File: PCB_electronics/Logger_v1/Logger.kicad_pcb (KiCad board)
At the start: 2 copper layers, 87.5 x 52.5 mm, 26 parts, among them P1 GPS_breakout_connector, P10 CONN_01X03, P11 CONN_01X02, P12 CONN_01X02, P13 CONN_01X02, P14 CONN_01X02, P15 CONN_01X02, P2 SD_breakout_connector, P3 Iridium_connector, P4 VN100_connector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

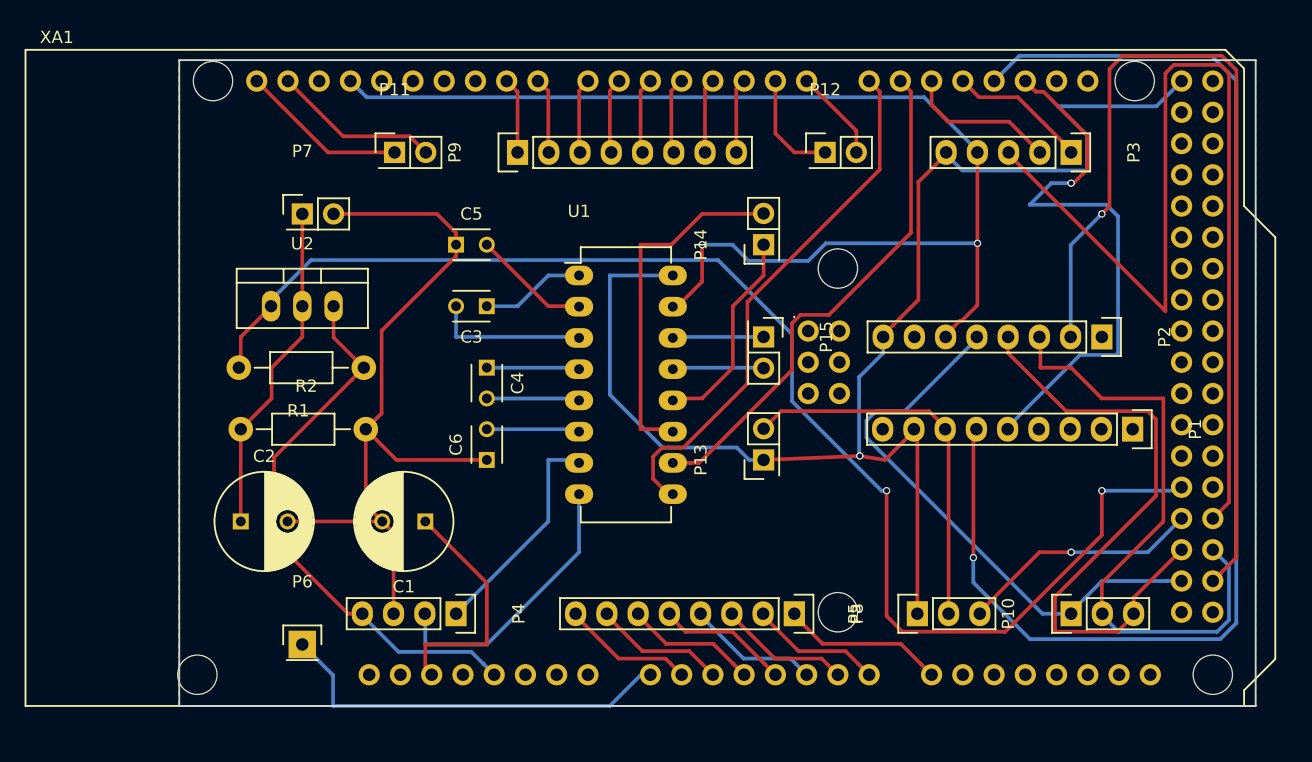
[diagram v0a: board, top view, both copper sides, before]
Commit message: corrected error on MAX232
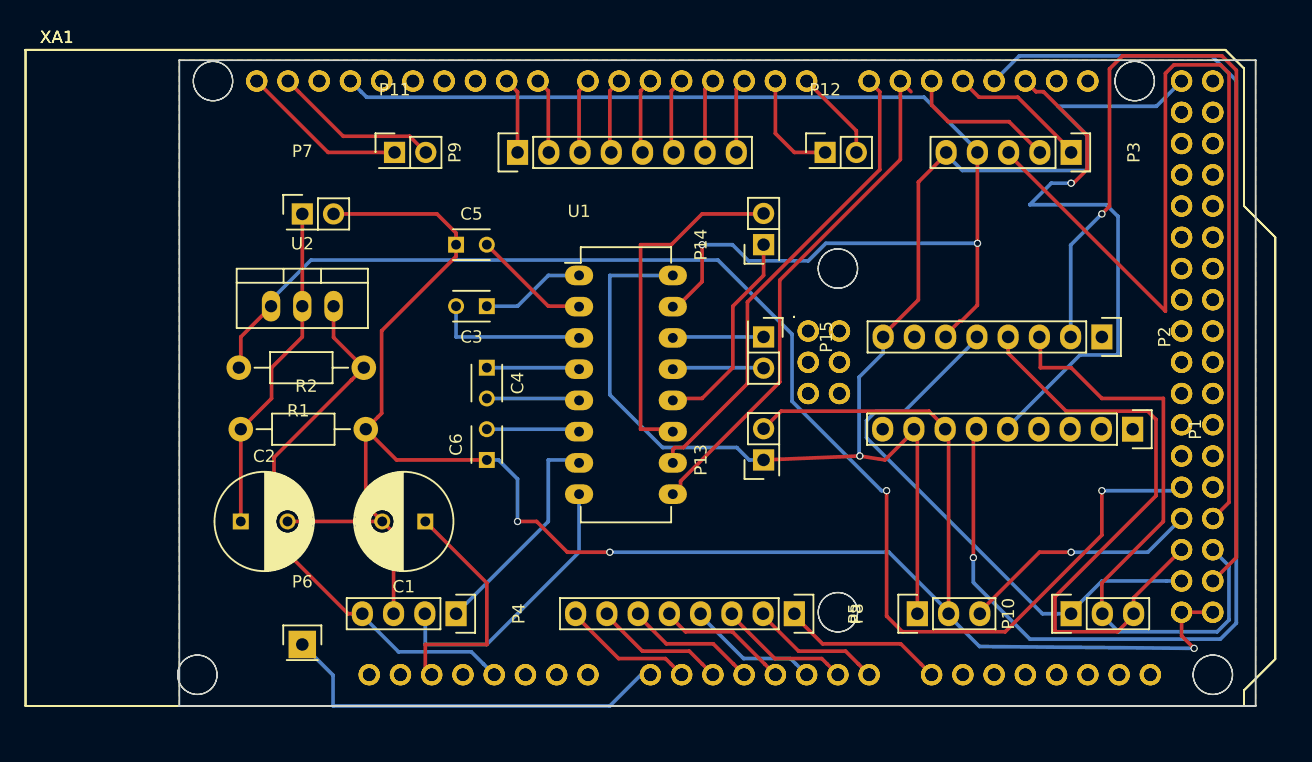
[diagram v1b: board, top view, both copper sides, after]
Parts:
- added XA1: Arduino_Mega2560_Shield, Arduino:Arduino_Mega2560_Shield, F.Cu at (112.5, 140.0)
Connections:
- U1 pad 10: /RX3 -> /TX3
- U1 pad 9: /TX3 -> /RX3
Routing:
- net GND: track 194.6 -> 266.5 mm, vias 2 -> 5
- net /TX3: track 43.5 -> 38.8 mm
- net /RX3: track 42.0 -> 42.7 mm

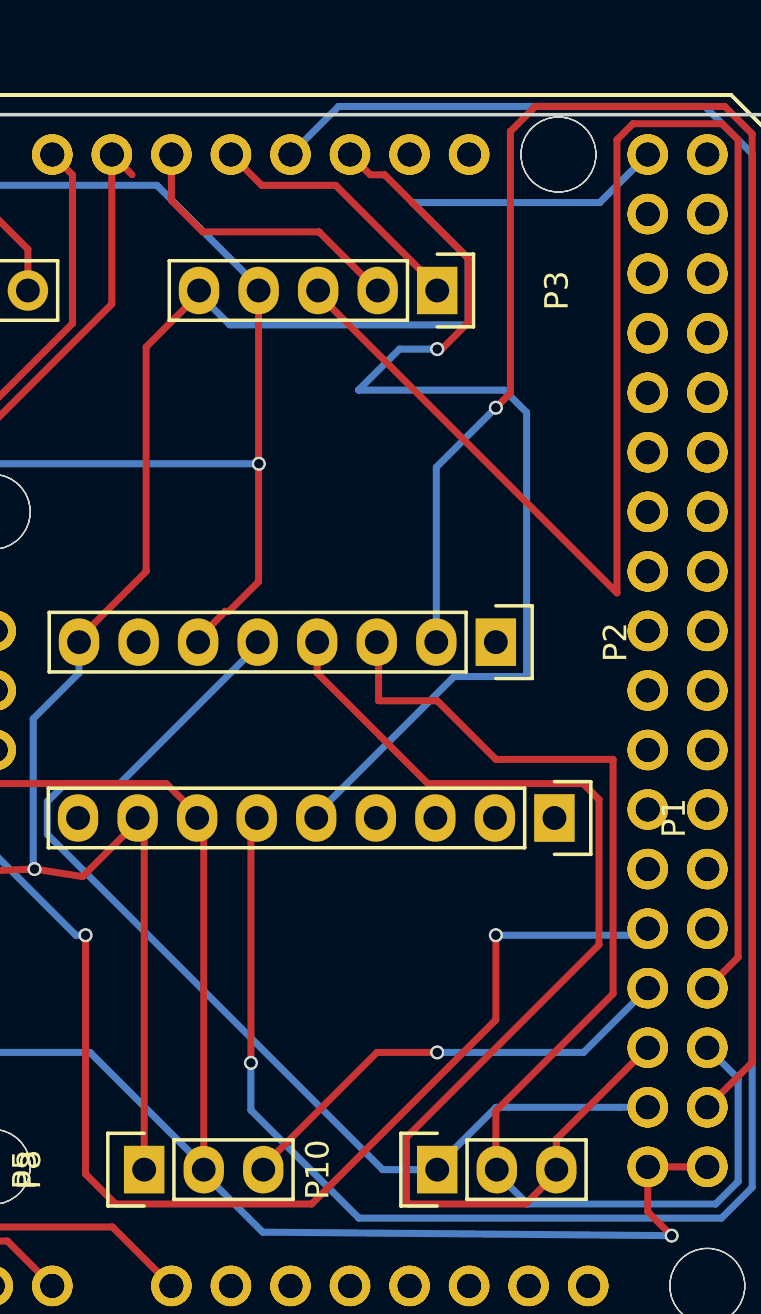
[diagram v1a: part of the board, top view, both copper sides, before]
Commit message: drc warning but should be ok
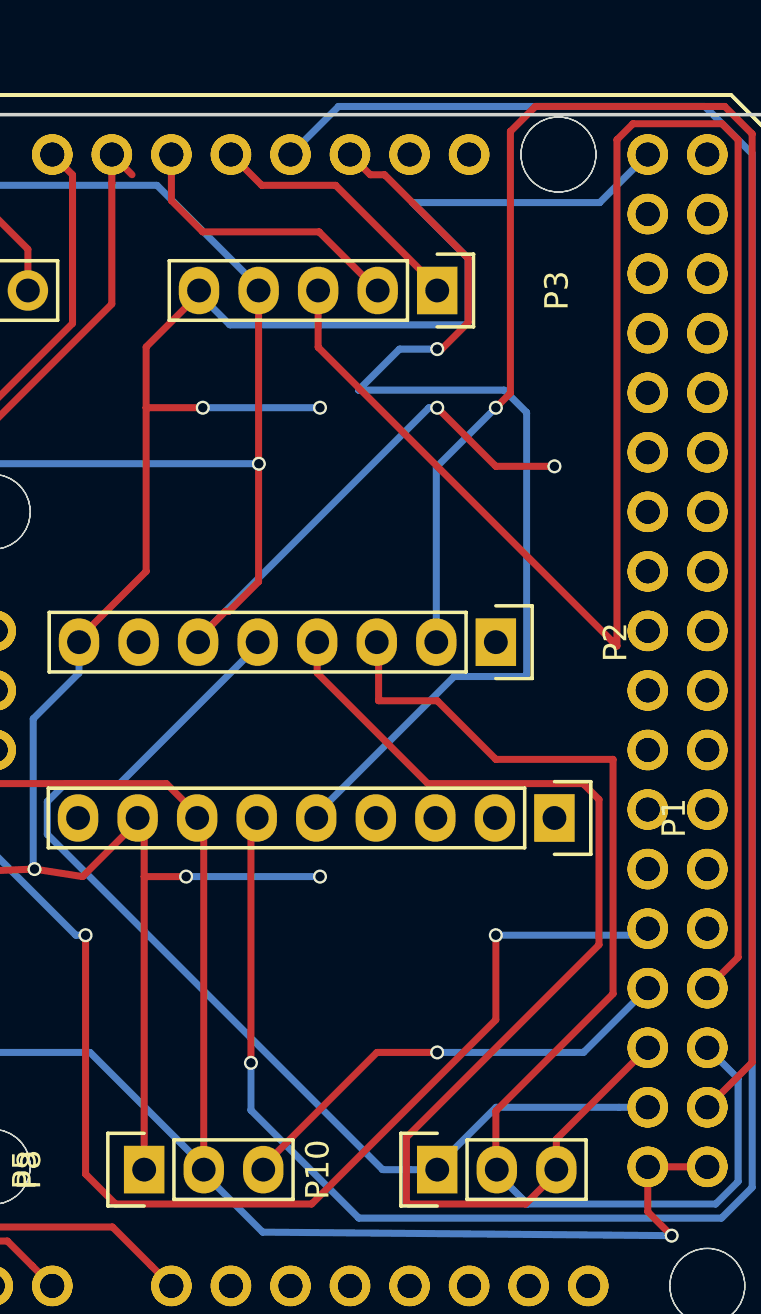
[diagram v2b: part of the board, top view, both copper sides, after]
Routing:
- net GND: track 266.5 -> 287.0 mm, vias 5 -> 7
- net +5V: track 160.4 -> 175.3 mm, vias 1 -> 5
- net /IRD_ON_OFF: track 80.0 -> 84.5 mm
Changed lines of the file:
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@@
 (kicad_pcb (version 4) (host pcbnew 4.0.2+dfsg1-stable)
   (general
-    (links 82)
+    (links 173)
     (no_connects 0)
     (area 124.924999 87.424999 212.575001 140.075001)
     (thickness 1.6)
     (drawings 4)
-    (tracks 369)
+    (tracks 386)
     (zones 0)
     (modules 27)
@@
   (gr_line (start 212.5 87.5) (end 212.5 140) (angle 90) (layer Edge.Cuts) (width 0.15))
   (gr_line (start 125 87.5) (end 212.5 87.5) (angle 90) (layer Edge.Cuts) (width 0.15))
+  (segment (start 197.5 100) (end 200 102.5) (width 0.3) (layer F.Cu) (net 49))
+  (segment (start 200 102.5) (end 202.5 102.5) (width 0.3) (layer F.Cu) (net 49))
+  (via (at 202.5 102.5) (size 0.6) (drill 0.4) (layers F.Cu B.Cu) (net 49))
+  (segment (start 197.1476 100) (end 197.5 100) (width 0.3) (layer B.Cu) (net 49))
+  (via (at 197.5 100) (size 0.6) (drill 0.4) (layers F.Cu B.Cu) (net 49))
+  (segment (start 187.3 110) (end 187.3 109.8476) (width 0.3) (layer B.Cu) (net 49))
+  (segment (start 187.3 109.8476) (end 197.1476 100) (width 0.3) (layer B.Cu) (net 49))
   (segment (start 190.053629 135.166029) (end 207.5 135.31603) (width 0.3) (layer B.Cu) (net 49))
   (segment (start 206.48 132.38) (end 206.48 134.29603) (width 0.3) (layer F.Cu) (net 49))
@@
   (segment (start 189.554603 129.964478) (end 189.554603 127.945402) (width 0.3) (layer B.Cu) (net 63))
   (via (at 189.554603 127.945402) (size 0.6) (drill 0.4) (layers F.Cu B.Cu) (net 63))
+  (segment (start 187.5 100) (end 192.5 100) (width 0.3) (layer B.Cu) (net 64))
+  (via (at 192.5 100) (size 0.6) (drill 0.4) (layers F.Cu B.Cu) (net 64))
+  (segment (start 185.083609 100) (end 185.083609 106.983991) (width 0.3) (layer F.Cu) (net 64))
+  (segment (start 185.083609 100) (end 187.5 100) (width 0.3) (layer F.Cu) (net 64))
+  (segment (start 185.083609 97.408791) (end 185.083609 100) (width 0.3) (layer F.Cu) (net 64))
+  (via (at 187.5 100) (size 0.6) (drill 0.4) (layers F.Cu B.Cu) (net 64))
+  (segment (start 186.78999 120) (end 192.5 120) (width 0.3) (layer B.Cu) (net 64))
+  (via (at 192.5 120) (size 0.6) (drill 0.4) (layers F.Cu B.Cu) (net 64))
+  (segment (start 185 120) (end 185 117.78) (width 0.3) (layer F.Cu) (net 64))
+  (segment (start 185 132.5) (end 185 120) (width 0.3) (layer F.Cu) (net 64))
+  (segment (start 185 120) (end 186.78999 120) (width 0.3) (layer F.Cu) (net 64))
+  (via (at 186.78999 120) (size 0.6) (drill 0.4) (layers F.Cu B.Cu) (net 64))
   (segment (start 206.48 89.2) (end 204.429999 91.250001) (width 0.3) (layer B.Cu) (net 64))
   (segment (start 204.429999 91.250001) (end 196.439603 91.250001) (width 0.3) (layer B.Cu) (net 64))
@@
   (segment (start 182.3724 120) (end 184.72 117.6524) (width 0.3) (layer F.Cu) (net 64))
   (segment (start 184.72 117.6524) (end 184.72 117.5) (width 0.3) (layer F.Cu) (net 64))
-  (segment (start 185 132.5) (end 185 117.78) (width 0.3) (layer F.Cu) (net 64))
   (segment (start 185 117.78) (end 184.72 117.5) (width 0.3) (layer F.Cu) (net 64))
   (segment (start 139.88 132.5) (end 139.88 132.6524) (width 0.3) (layer B.Cu) (net 64))
@@
   (segment (start 187.34 95) (end 187.34 95.1524) (width 0.3) (layer F.Cu) (net 64))
   (segment (start 187.34 95.1524) (end 185.083609 97.408791) (width 0.3) (layer F.Cu) (net 64))
-  (segment (start 185.083609 97.408791) (end 185.083609 106.983991) (width 0.3) (layer F.Cu) (net 64))
   (segment (start 185.083609 106.983991) (end 182.22 109.8476) (width 0.3) (layer F.Cu) (net 64))
   (segment (start 182.22 109.8476) (end 182.22 110) (width 0.3) (layer F.Cu) (net 64))
@@
   (segment (start 187.5 92.5) (end 192.46 92.5) (width 0.3) (layer F.Cu) (net 73))
   (segment (start 186.16 91.16) (end 187.5 92.5) (width 0.3) (layer F.Cu) (net 73))
-  (segment (start 192.42 95) (end 192.42 95.1524) (width 0.3) (layer F.Cu) (net 74))
-  (segment (start 192.42 95.1524) (end 205.166399 107.898799) (width 0.3) (layer F.Cu) (net 74))
-  (segment (start 210.333601 88.569471) (end 210.333601 123.446399) (width 0.3) (layer F.Cu) (net 74))
-  (segment (start 205.166399 107.898799) (end 205.166399 88.569471) (width 0.3) (layer F.Cu) (net 74))
+  (segment (start 192.42 95) (end 192.42 97.42) (width 0.3) (layer F.Cu) (net 74))
+  (segment (start 192.42 97.42) (end 205.166399 110.166399) (width 0.3) (layer F.Cu) (net 74))
+  (segment (start 205.166399 110.166399) (end 205.166399 88.569471) (width 0.3) (layer F.Cu) (net 74))
   (segment (start 205.166399 88.569471) (end 205.849471 87.886399) (width 0.3) (layer F.Cu) (net 74))
   (segment (start 205.849471 87.886399) (end 209.650529 87.886399) (width 0.3) (layer F.Cu) (net 74))
   (segment (start 209.650529 87.886399) (end 210.333601 88.569471) (width 0.3) (layer F.Cu) (net 74))
   (segment (start 210.333601 123.446399) (end 209.02 124.76) (width 0.3) (layer F.Cu) (net 74))
+  (segment (start 210.333601 88.569471) (end 210.333601 123.446399) (width 0.3) (layer F.Cu) (net 74))
   (segment (start 157.5 120.24) (end 157.5 120) (width 0.3) (layer B.Cu) (net 75) (status 80000))
   (segment (start 157.5 120) (end 155 120) (width 0.3) (layer B.Cu) (net 75) (status 80000))

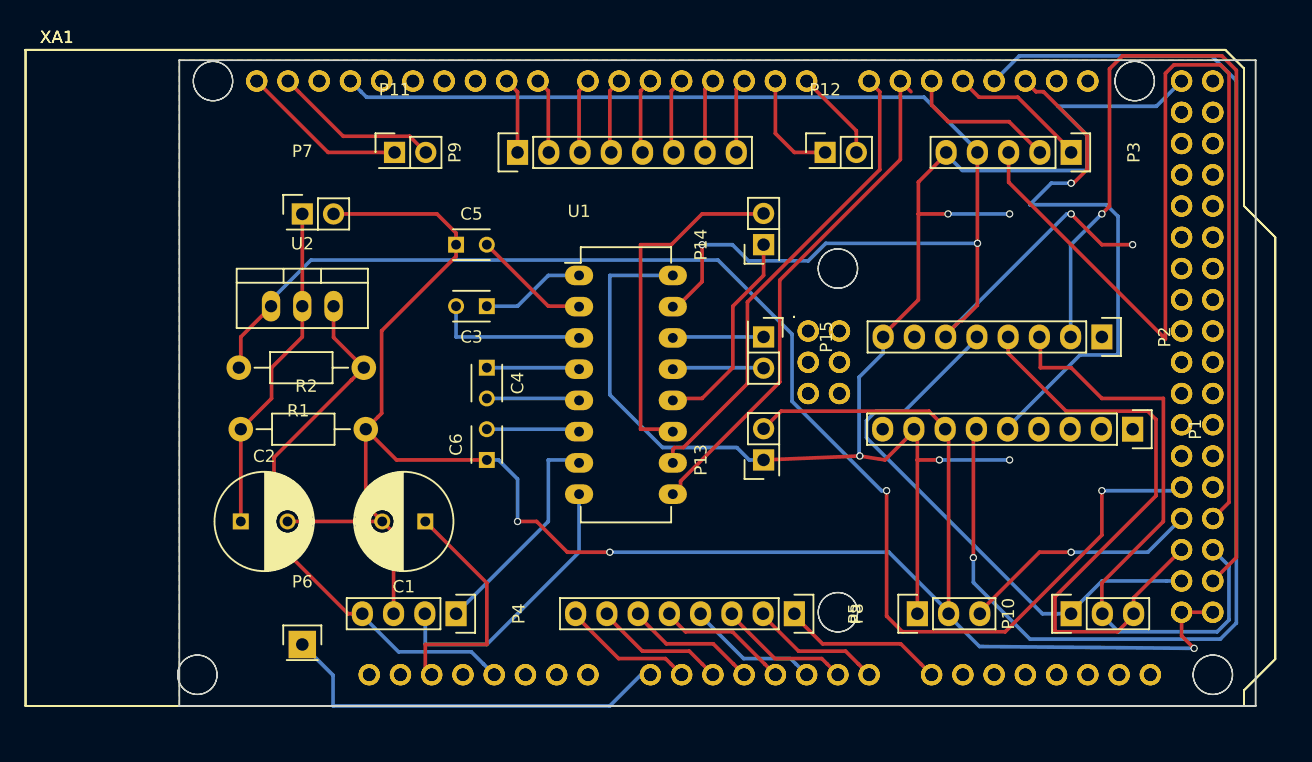
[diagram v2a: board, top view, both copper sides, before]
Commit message: extended slightly the board
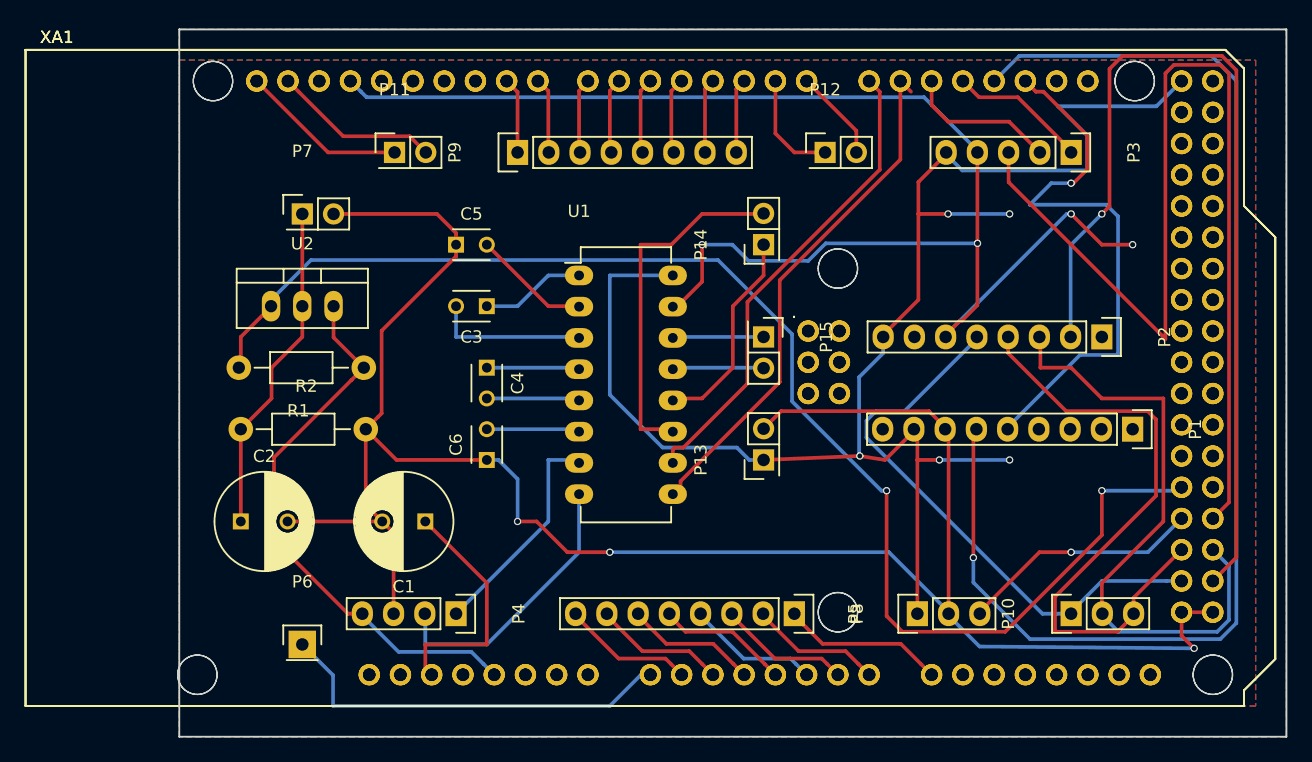
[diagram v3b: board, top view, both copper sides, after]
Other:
- board size 87.5 x 52.5 mm -> 90 x 57.5 mm
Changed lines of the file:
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@@
   (page A4)
   (layers
-    (0 F.Cu signal)
+    (0 F.Cu signal hide)
     (31 B.Cu signal)
     (32 B.Adhes user)
@@
     )
   )
-  (gr_line (start 125 140) (end 125 87.5) (angle 90) (layer Edge.Cuts) (width 0.15))
-  (gr_line (start 212.5 140) (end 125 140) (angle 90) (layer Edge.Cuts) (width 0.15))
-  (gr_line (start 212.5 87.5) (end 212.5 140) (angle 90) (layer Edge.Cuts) (width 0.15))
-  (gr_line (start 125 87.5) (end 212.5 87.5) (angle 90) (layer Edge.Cuts) (width 0.15))
+  (gr_line (start 215 85) (end 125 85) (layer Edge.Cuts) (width 0.15))
+  (gr_line (start 215 142.5) (end 215 85) (layer Edge.Cuts) (width 0.15))
+  (gr_line (start 125 142.5) (end 215 142.5) (layer Edge.Cuts) (width 0.15))
+  (gr_line (start 125 85) (end 125 142.5) (layer Edge.Cuts) (width 0.15))
   (segment (start 197.5 100) (end 200 102.5) (width 0.3) (layer F.Cu) (net 49))
   (segment (start 200 102.5) (end 202.5 102.5) (width 0.3) (layer F.Cu) (net 49))
@@
       )
     )
+  )
+  (zone (net 64) (net_name +5V) (layer F.Cu) (hatch edge 0.508)
+    (connect_pads (clearance 0.508))
+    (min_thickness 0.254)
+    (fill yes (arc_segments 16) (thermal_gap 0.508) (thermal_bridge_width 0.508))
+    (polygon
+      (pts
+        (xy 125 85) (xy 215 85) (xy 215 142.5) (xy 125 142.5)
+      )
+    )
+  )
+  (zone (net 49) (net_name GND) (layer B.Cu) (hatch edge 0.508)
+    (connect_pads (clearance 0.508))
+    (min_thickness 0.254)
+    (fill yes (arc_segments 16) (thermal_gap 0.508) (thermal_bridge_width 0.508))
+    (polygon
+      (pts
+        (xy 125 85) (xy 215 85) (xy 215 142.5) (xy 125 142.5)
+      )
+    )
